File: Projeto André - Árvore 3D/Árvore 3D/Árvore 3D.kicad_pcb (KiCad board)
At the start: 2 copper layers, 97.8 x 99.1 mm, 58 parts, among them J1 Conn_01x03_Pin, J10 TestPoint, J11 TestPoint, J12 TestPoint, J13 TestPoint, J14 TestPoint, J15 TestPoint, J16 TestPoint, J17 TestPoint, J18 TestPoint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

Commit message: Revisão do projeto e inclusão de logos.
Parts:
- added G***: LOGO, LOGO, F.Cu at (140.2, 85.9)
- added G***: LOGO, LOGO, F.Cu at (140.2, 95.5)
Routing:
- net GND: track 391.4 -> 392.2 mm, vias 18 -> 38
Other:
- outline, holes or cut-outs redrawn
- board text added: "André Araújo Árvore de Natal 3D Rev.00"
- board text added: "Feliz Natal! Jesus nasceu!"

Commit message: Finalização da versão inicial - Rev.00
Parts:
- added G***: LOGO, LOGO, F.Cu at (178.3, 62.2)
- added G***: LOGO, LOGO, F.Cu at (196.8, 83.1)
- added G***: LOGO, LOGO, F.Cu at (155.4, 70.1)
- added G***: LOGO, LOGO, F.Cu at (169.4, 42.4)
- added G***: LOGO, LOGO, F.Cu at (173.7, 71.9)
- added G***: LOGO, LOGO, F.Cu at (177.3, 98.3)
- added G***: LOGO, LOGO, F.Cu at (193.0, 45.7)
- added G***: LOGO, LOGO, F.Cu at (197.4, 74.4)
- added G***: LOGO, LOGO, F.Cu at (165.1, 96.5)
- added G***: LOGO, LOGO, B.Cu at (177.5, 108.0)
- added G***: LOGO, LOGO, F.Cu at (155.7, 98.8)
- added G***: LOGO, LOGO, B.Cu at (145.5, 63.0)
- added G***: LOGO, LOGO, B.Cu at (126.7, 118.1)
- added G***: LOGO, LOGO, B.Cu at (142.0, 94.2)
- added G***: LOGO, LOGO, B.Cu at (205.7, 47.0)
- added G***: LOGO, LOGO, B.Cu at (156.2, 132.1)
- added G***: LOGO, LOGO, B.Cu at (159.3, 116.6)
- added G***: LOGO, LOGO, B.Cu at (197.4, 74.7)
- added G***: LOGO, LOGO, B.Cu at (185.7, 117.6)
- added G***: LOGO, LOGO, B.Cu at (173.7, 72.9)
- added G***: LOGO, LOGO, B.Cu at (155.4, 71.9)
- added G***: LOGO, LOGO, F.Cu at (202.9, 44.5)
- added G***: LOGO, LOGO, B.Cu at (141.0, 132.1)
- added G***: LOGO, LOGO, B.Cu at (195.8, 84.6)
- added G***: LOGO, LOGO, B.Cu at (158.8, 98.6)
- added G***: LOGO, LOGO, B.Cu at (169.7, 121.4)
- added G***: LOGO, LOGO, B.Cu at (164.3, 68.6)
- added G***: LOGO, LOGO, B.Cu at (169.2, 43.9)
- added G***: LOGO, LOGO, B.Cu at (175.8, 133.6)
- added G***: LOGO, LOGO, B.Cu at (193.3, 46.0)
- added G***: LOGO, LOGO, B.Cu at (154.9, 86.1)
- added G***: LOGO, LOGO, B.Cu at (178.1, 98.8)
- added G***: LOGO, LOGO, F.Cu at (184.7, 115.8)
- added G***: LOGO, LOGO, B.Cu at (176.3, 61.5)
- added G***: LOGO, LOGO, B.Cu at (189.0, 57.1)
- added G***: LOGO, LOGO, B.Cu at (138.7, 113.8)
- added G***: LOGO, LOGO, F.Cu at (164.6, 68.6)
- added G***: LOGO, LOGO, F.Cu at (177.0, 105.9)
- added G***: LOGO, LOGO, F.Cu at (188.7, 54.6)
- added G***: LOGO, LOGO, F.Cu at (145.5, 61.2)
- added REF**: OSHW-Logo2_7.3x6mm_SilkScreen, Symbol:OSHW-Logo2_7.3x6mm_SilkScreen, F.Cu at (139.4, 83.8)
- moved G*** 41.6 mm to (122.4, 133.1)
- moved G*** 6.71 mm to (137.4, 91.9)
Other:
- board text added: "Projeto Natal 2023"

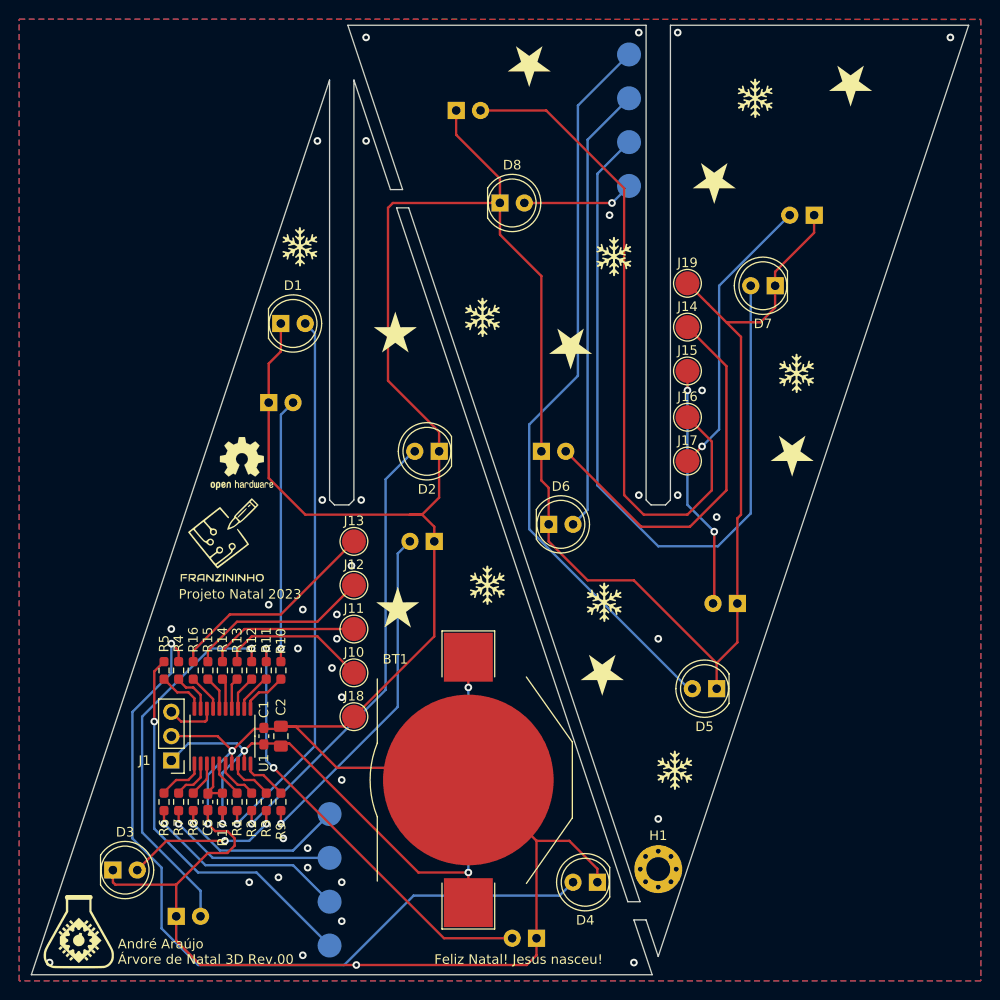
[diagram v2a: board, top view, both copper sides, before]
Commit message: Início da Rev.01. Inclusão de Test Points. Inclusão de botão e inclusão do arquivo 3D do suporte de bateria. Melhorias gerais.
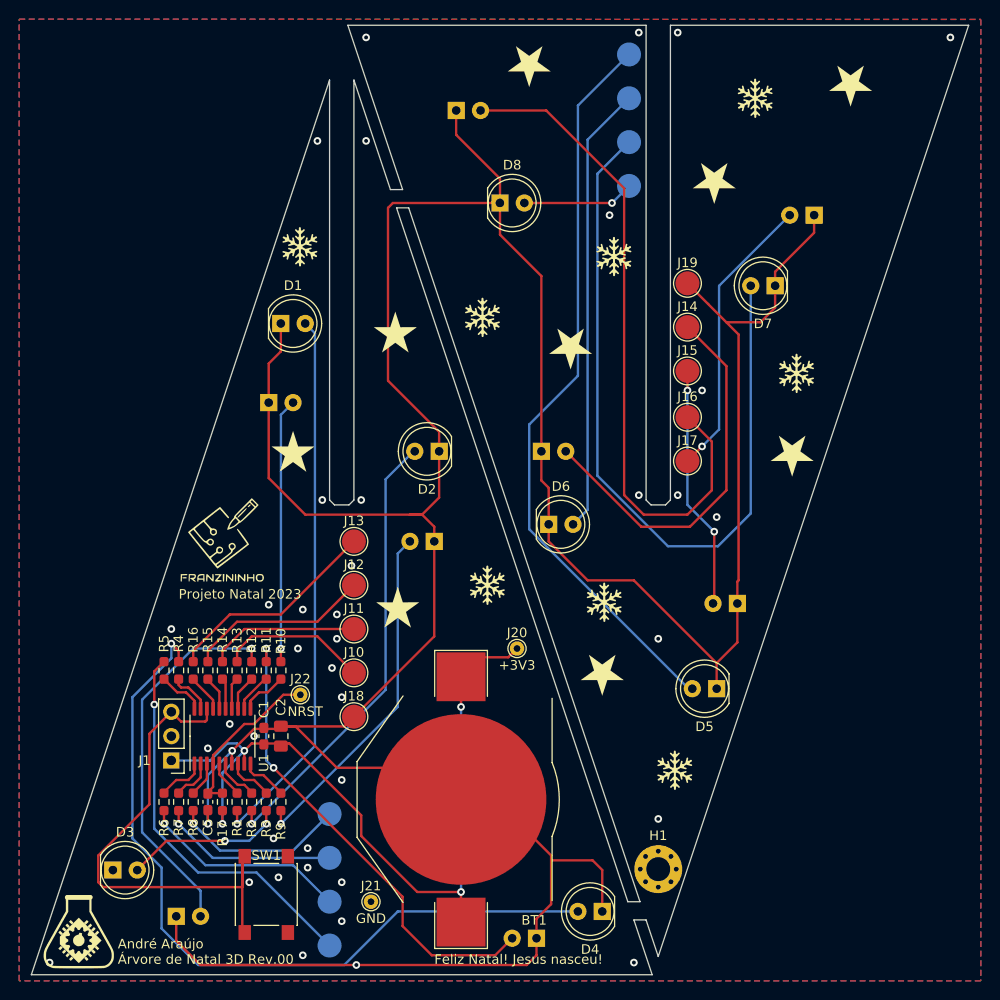
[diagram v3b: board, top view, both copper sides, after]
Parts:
- removed REF**: OSHW-Logo2_7.3x6mm_SilkScreen, Symbol:OSHW-Logo2_7.3x6mm_SilkScreen
- added G***: LOGO, LOGO, F.Cu at (144.8, 82.5)
- added J20: +3V3, TestPoint:TestPoint_THTPad_D1.5mm_Drill0.7mm, F.Cu at (168.1, 103.1)
- added J21: GND, TestPoint:TestPoint_THTPad_D1.5mm_Drill0.7mm, F.Cu at (152.9, 129.5)
- added J22: NRST, TestPoint:TestPoint_THTPad_D1.5mm_Drill0.7mm, F.Cu at (145.5, 108.0)
- added SW1: SW_Push, Button_Switch_SMD:SW_Push_1P1T_NO_6x6mm_H9.5mm, F.Cu at (142.0, 128.8)
- moved G*** 6.93 mm to (170.7, 114.6)
- moved G*** 6.73 mm to (174.5, 127.0)
- moved D4 3.09 mm to (177.0, 130.6)
- moved BT1 2.17 mm to (162.3, 118.9), turned to -90 degrees
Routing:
- net SWIO: track 5.38 -> 52.7 mm
- net GND: track 391.9 -> 363.9 mm, vias 38 -> 41
- net Net-(U1-NRST/PD7): track 4.91 -> 17.5 mm
- net +3V3: track 76.3 -> 81.6 mm
- net LED11: track 46.4 -> 49.7 mm
- net LED12: track 39.1 -> 40.1 mm
- net LED4: track 83.1 -> 82.2 mm
- net Net-(D7-A): track 81.0 -> 80.4 mm

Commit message: Finalização da Rev.01. Elaboração de arquivos de fabricação.
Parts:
- added R18: 10K, Resistor_SMD:R_0603_1608Metric_Pad0.98x0.95mm_HandSolder, F.Cu at (142.0, 123.4)
- SW1: footprint Button_Switch_SMD:SW_Push_1P1T_NO_6x6mm_H9.5mm -> Button_Switch_SMD:SW_Push_1P1T_NO_CK_KSC6xxJ
- moved G*** 18.1 mm to (159.8, 79.2)
- moved D1 14.1 mm to (142.5, 83.3)
- moved D10 13.2 mm to (142.7, 90.7)
- moved D15 12.2 mm to (161.8, 59.2)
- moved G*** 10.8 mm to (138.4, 84.1)
- moved G*** 9.65 mm to (144.8, 72.9)
- moved G*** 9.52 mm to (165.1, 97.3)
- moved D14 7.73 mm to (189.2, 105.9)
- moved D8 6.90 mm to (165.6, 63.5)
- moved D7 6.75 mm to (201.4, 67.6)
- moved D16 5.08 mm to (203.2, 61.0)
- moved G*** 4.83 mm to (155.2, 65.3)
- moved D5 4.01 mm to (188.2, 111.3)
- moved G*** 3.94 mm to (146.6, 57.4)
- moved D13 2.79 mm to (170.7, 85.3)
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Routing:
- net LED1: track 57.4 -> 43.7 mm
- net LED10: track 27.6 -> 14.6 mm
- net GND: track 363.9 -> 351.8 mm
- net Net-(D14-A): track 25.5 -> 31.7 mm
- net +3V3: track 81.6 -> 86.1 mm
- net SWIO: track 52.7 -> 57.1 mm
- net Net-(D8-A): track 11.7 -> 15.9 mm
- net Net-(D5-A): track 77.8 -> 81.5 mm
- net LED2: track 47.4 -> 44.9 mm
- net LED9: track 36.4 -> 38.5 mm
- net Net-(D6-A): track 46.9 -> 48.5 mm
- net LED11: track 49.7 -> 50.9 mm
- net Net-(D16-A): track 30.1 -> 28.9 mm
- net Net-(D13-A): track 40.3 -> 39.1 mm
- net Net-(D15-A): track 70.1 -> 69.0 mm
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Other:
- outline, holes or cut-outs redrawn
- board text added: "André Araújo Árvore de Natal 3D Rev.01"
- board text removed: "André Araújo Árvore de Natal 3D Rev.00"
